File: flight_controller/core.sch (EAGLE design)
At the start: 103 parts, among them J1 M02, J13 MOLEX-3POS, J14 MOLEX-3POS, J15 MOLEX-4POS, J16 MOLEX-3POS, J17 M03, J18 M04, J19 MOLEX-3POS, J2 MOLEX-2POS, J20 MOLEX-4POS, J3 MOLEX-2POS, J4 MOLEX-2POS, J5 MOLEX-2POS, J6 MOLEX-2POS, J7 MOLEX-2POS, J8 MOLEX-2POS, J9 MOLEX-2POS, Q10 EM6K1, Q11 EM6K1, Q2 200mA/50V, Q5 200mA/50V, Q6 200mA/50V, Q7 EM6K1, Q8 EM6K1, U1 MPU-6000QFN-24, U2 MEAS-MS5611, U3 USD-SOCKETNEW, U4 STM32F405, U5 MIC5219 3.3V, Y1 16MHz

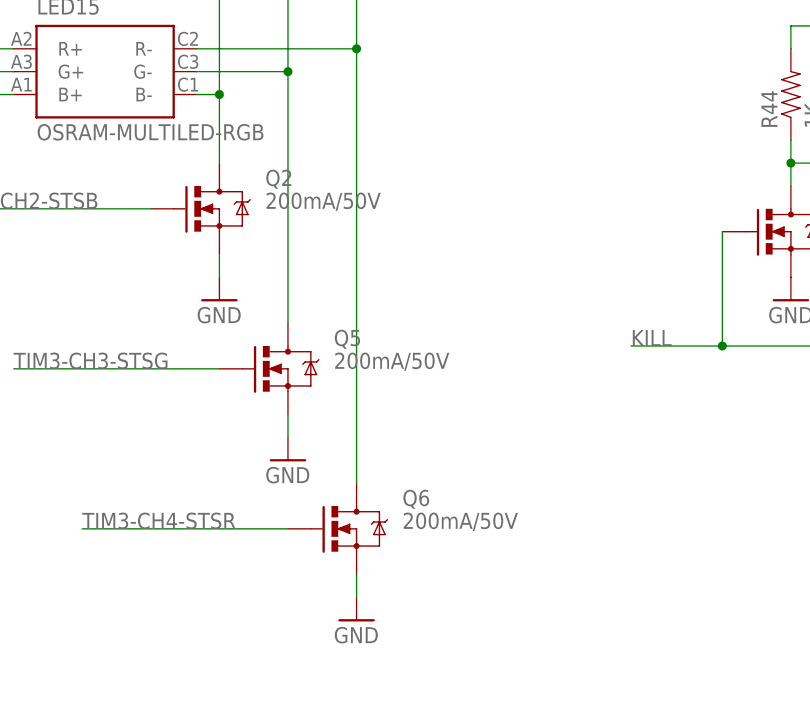
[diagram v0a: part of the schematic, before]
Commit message: Replace LED MOSFETs with dual-channel MOSFETs.
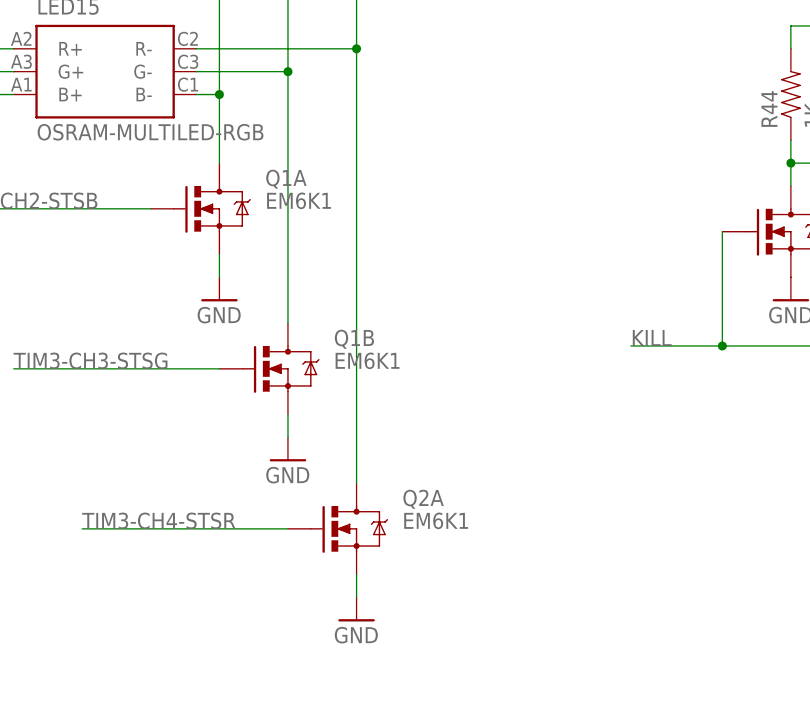
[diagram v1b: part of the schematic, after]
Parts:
- removed Q5, Q6: 200mA/50V, SparkFun-DiscreteSemi:MOSFET-NCHANNELBSS138
- added Q1: EM6K1, OSURC_DiscreteSemi:MOSFET-NCHANNEL-DUALEM6K1
- Q2: value 200mA/50V -> EM6K1; device SparkFun-DiscreteSemi:MOSFET-NCHANNELBSS138 -> OSURC_DiscreteSemi:MOSFET-NCHANNEL-DUALEM6K1
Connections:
- net GND: now also Q1A.S, Q1B.S, Q2A.S; no longer Q2.S, Q5.S, Q6.S
- net N$5: now also Q1A.D; no longer Q2.D
- net N$6: now also Q1B.D; no longer Q5.D
- net N$7: now also Q2A.D; no longer Q6.D
- net TIM3-CH2-STSB: now also Q1A.G; no longer Q2.G
- net TIM3-CH3-STSG: now also Q1B.G; no longer Q5.G
- net TIM3-CH4-STSR: now also Q2A.G; no longer Q6.G
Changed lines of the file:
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@@
 <part name="LED7" library="SparkFun-LED" deviceset="LED" device="0603" value="ORANGE"/>
 <part name="LED14" library="OSURC_LED" deviceset="OSRAM-MULTILED-RGB" device=""/>
-<part name="Q2" library="SparkFun-DiscreteSemi" deviceset="MOSFET-NCHANNEL" device="BSS138" value="200mA/50V"/>
-<part name="Q5" library="SparkFun-DiscreteSemi" deviceset="MOSFET-NCHANNEL" device="BSS138" value="200mA/50V"/>
-<part name="Q6" library="SparkFun-DiscreteSemi" deviceset="MOSFET-NCHANNEL" device="BSS138" value="200mA/50V"/>
 <part name="LED15" library="OSURC_LED" deviceset="OSRAM-MULTILED-RGB" device=""/>
 <part name="GND14" library="SparkFun-Aesthetics" deviceset="GND" device=""/>
@@
 <part name="R48" library="SparkFun" deviceset="RESISTOR" device="0603-RES" value="1K"/>
 <part name="SUPPLY18" library="SparkFun-Aesthetics" deviceset="3.3V" device=""/>
+<part name="Q1" library="OSURC_DiscreteSemi" deviceset="MOSFET-NCHANNEL-DUAL" device="EM6K1" value="EM6K1"/>
+<part name="Q2" library="OSURC_DiscreteSemi" deviceset="MOSFET-NCHANNEL-DUAL" device="EM6K1" value="EM6K1"/>
 </parts>
 <sheets>
@@
 <instance part="LED7" gate="G$1" x="154.94" y="172.72" rot="R90"/>
 <instance part="LED14" gate="G$1" x="254" y="220.98"/>
-<instance part="Q2" gate="G$1" x="266.7" y="182.88"/>
-<instance part="Q5" gate="G$1" x="274.32" y="165.1"/>
-<instance part="Q6" gate="G$1" x="281.94" y="147.32"/>
 <instance part="LED15" gate="G$1" x="254" y="198.12"/>
 <instance part="GND14" gate="1" x="266.7" y="172.72"/>
@@
 <instance part="R48" gate="G$1" x="322.58" y="238.76" rot="R90"/>
 <instance part="SUPPLY18" gate="G$1" x="322.58" y="246.38"/>
+<instance part="Q1" gate="A" x="266.7" y="182.88"/>
+<instance part="Q1" gate="B" x="274.32" y="165.1"/>
+<instance part="Q2" gate="A" x="281.94" y="147.32"/>
 </instances>
 <busses>
@@
 </segment>
 <segment>
-<pinref part="Q2" gate="G$1" pin="S"/>
 <pinref part="GND14" gate="1" pin="GND"/>
 <wire x1="266.7" y1="175.26" x2="266.7" y2="177.8" width="0.1524" layer="91"/>
-</segment>
-<segment>
-<pinref part="Q5" gate="G$1" pin="S"/>
+<pinref part="Q1" gate="A" pin="S"/>
+</segment>
+<segment>
 <pinref part="GND28" gate="1" pin="GND"/>
 <wire x1="274.32" y1="157.48" x2="274.32" y2="160.02" width="0.1524" layer="91"/>
-</segment>
-<segment>
-<pinref part="Q6" gate="G$1" pin="S"/>
+<pinref part="Q1" gate="B" pin="S"/>
+</segment>
+<segment>
 <pinref part="GND29" gate="1" pin="GND"/>
 <wire x1="281.94" y1="139.7" x2="281.94" y2="142.24" width="0.1524" layer="91"/>
+<pinref part="Q2" gate="A" pin="S"/>
 </segment>
 <segment>
@@
 <wire x1="266.7" y1="165.1" x2="243.84" y2="165.1" width="0.1524" layer="91"/>
 <label x="243.84" y="165.1" size="1.778" layer="95"/>
-<pinref part="Q5" gate="G$1" pin="G"/>
+<pinref part="Q1" gate="B" pin="G"/>
 </segment>
 </net>
@@
 <segment>
 <pinref part="LED15" gate="G$1" pin="B-"/>
-<pinref part="Q2" gate="G$1" pin="D"/>
 <wire x1="264.16" y1="195.58" x2="266.7" y2="195.58" width="0.1524" layer="91"/>
 <wire x1="266.7" y1="195.58" x2="266.7" y2="187.96" width="0.1524" layer="91"/>
@@
 <wire x1="266.7" y1="218.44" x2="266.7" y2="195.58" width="0.1524" layer="91"/>
 <junction x="266.7" y="195.58"/>
+<pinref part="Q1" gate="A" pin="D"/>
 </segment>
 </net>
@@
 <segment>
 <pinref part="LED15" gate="G$1" pin="G-"/>
-<pinref part="Q5" gate="G$1" pin="D"/>
 <wire x1="264.16" y1="198.12" x2="274.32" y2="198.12" width="0.1524" layer="91"/>
 <wire x1="274.32" y1="198.12" x2="274.32" y2="170.18" width="0.1524" layer="91"/>
@@
 <wire x1="274.32" y1="220.98" x2="274.32" y2="198.12" width="0.1524" layer="91"/>
 <junction x="274.32" y="198.12"/>
+<pinref part="Q1" gate="B" pin="D"/>
 </segment>
 </net>
@@
 <segment>
 <pinref part="LED15" gate="G$1" pin="R-"/>
-<pinref part="Q6" gate="G$1" pin="D"/>
 <wire x1="264.16" y1="200.66" x2="281.94" y2="200.66" width="0.1524" layer="91"/>
 <wire x1="281.94" y1="200.66" x2="281.94" y2="152.4" width="0.1524" layer="91"/>
@@
 <wire x1="281.94" y1="223.52" x2="281.94" y2="200.66" width="0.1524" layer="91"/>
 <junction x="281.94" y="200.66"/>
+<pinref part="Q2" gate="A" pin="D"/>
 </segment>
 </net>
@@
 <wire x1="236.22" y1="182.88" x2="259.08" y2="182.88" width="0.1524" layer="91"/>
 <label x="236.22" y="182.88" size="1.778" layer="95"/>
-<pinref part="Q2" gate="G$1" pin="G"/>
+<pinref part="Q1" gate="A" pin="G"/>
 </segment>
 </net>
@@
 <wire x1="274.32" y1="147.32" x2="251.46" y2="147.32" width="0.1524" layer="91"/>
 <label x="251.46" y="147.32" size="1.778" layer="95"/>
-<pinref part="Q6" gate="G$1" pin="G"/>
-</segment>
-</net>
+<pinref part="Q2" gate="A" pin="G"/>
+</segment>
+</net>

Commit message: Remove 5V regulator todo and add reverse voltage protection.
Board will need 5V input from external regulator.
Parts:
- added J10: MOLEX-2POS, aerial:MOLEX-2POS
- added Q3: MOSFET-PCHANNEL-AON6407, OSURC_DiscreteSemi:MOSFET-PCHANNEL-AON6407
- Q1, Q10, Q11, Q2, Q7, Q8: device OSURC_DiscreteSemi:MOSFET-NCHANNEL-DUALEM6K1 -> OSURC_DiscreteSemi:MOSFET-NCHANNEL-DUAL-EM6K1
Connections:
- new net VIN: J10.1, Q3.D
- net 5V: now also Q3.S
- net GND: now also J10.2, Q3.G
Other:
- note added: "1K pullup on KILL pulls TIM1 and TIM4 channels down until the XBee deasserts KILL."
- note added: "5V in"
- note added: "Protection"
- note added: "Reverse Voltage"
- note added: "TODO: consider replacing with Molex Duraclik"
- note added: "TVS"
- note removed: "1K pullup on KILL keeps these N-ch MOSFETS on, pulling TIM1 and TIM4 channels down, until the XBee deasserts KILL."
- note removed: "5V REG"

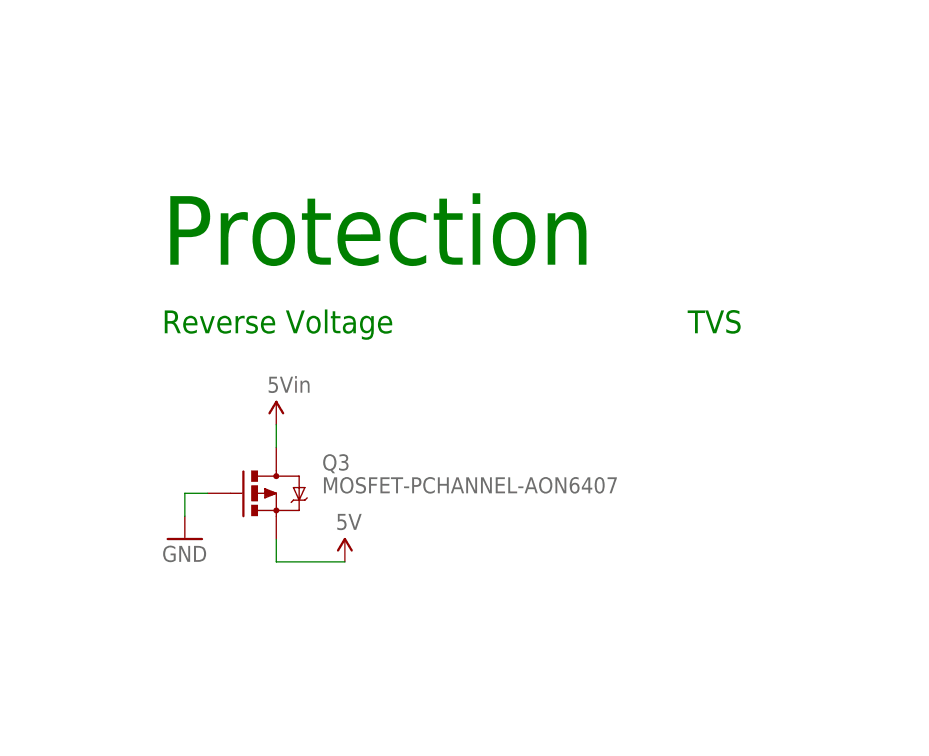
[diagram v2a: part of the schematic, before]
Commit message: Add TVS/RVP circuit.
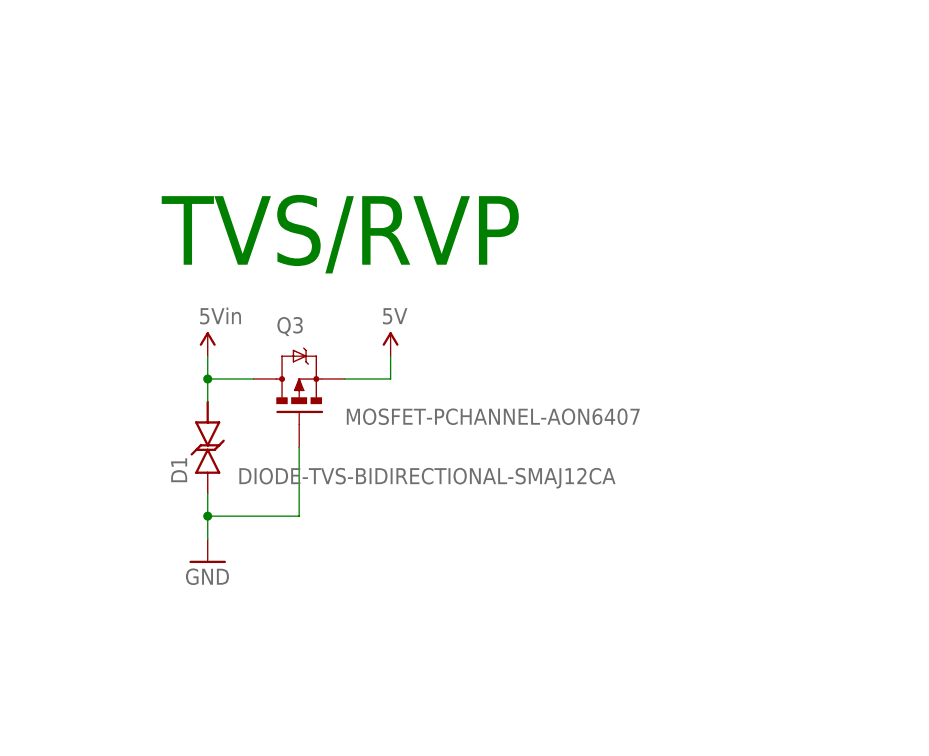
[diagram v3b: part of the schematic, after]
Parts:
- added D1: DIODE-TVS-BIDIRECTIONAL-SMAJ12CA, OSURC_DiscreteSemi:DIODE-TVS-BIDIRECTIONAL-SMAJ12CA
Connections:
- net GND: now also D1.1
- net VIN: now also D1.2
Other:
- note added: "TVS/RVP"
- note removed: "Protection"
- note removed: "Reverse Voltage"
- note removed: "TVS"
- moved on the sheet: Q3
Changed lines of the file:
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@@
 <part name="GND22" library="SparkFun-Aesthetics" deviceset="GND" device=""/>
 <part name="SUPPLY22" library="SparkFun-Aesthetics" deviceset="VIN" device="" value="5Vin"/>
+<part name="D1" library="OSURC_DiscreteSemi" deviceset="DIODE-TVS-BIDIRECTIONAL" device="-SMAJ12CA"/>
 </parts>
 <sheets>
@@
 the XBee deasserts KILL.</text>
 <text x="317.5" y="-403.86" size="7.62" layer="91">5V in</text>
-<text x="129.54" y="-73.66" size="7.62" layer="91">Protection</text>
+<text x="129.54" y="-73.66" size="7.62" layer="91">TVS/RVP</text>
 <text x="317.5" y="-439.42" size="1.778" layer="98">TODO: consider replacing with Molex Duraclik</text>
-<text x="129.54" y="-81.28" size="2.54" layer="91">Reverse Voltage</text>
-<text x="187.96" y="-81.28" size="2.54" layer="91">TVS</text>
 </plain>
 <instances>
@@
 <instance part="J10" gate="G$1" x="327.66" y="-421.64"/>
 <instance part="GND9" gate="1" x="320.04" y="-429.26"/>
-<instance part="Q3" gate="G$1" x="142.24" y="-99.06"/>
-<instance part="SUPPLY19" gate="G$1" x="142.24" y="-91.44"/>
-<instance part="SUPPLY21" gate="G$1" x="149.86" y="-106.68"/>
-<instance part="GND22" gate="1" x="132.08" y="-104.14"/>
+<instance part="Q3" gate="G$1" x="144.78" y="-86.36" smashed="yes" rot="R90">
+<attribute name="NAME" x="142.24" y="-81.28" size="1.778" layer="95"/>
+<attribute name="VALUE" x="149.86" y="-91.44" size="1.778" layer="96"/>
+</instance>
+<instance part="SUPPLY19" gate="G$1" x="134.62" y="-83.82"/>
+<instance part="SUPPLY21" gate="G$1" x="154.94" y="-83.82"/>
+<instance part="GND22" gate="1" x="134.62" y="-106.68"/>
 <instance part="SUPPLY22" gate="G$1" x="320.04" y="-414.02"/>
+<instance part="D1" gate="G$1" x="134.62" y="-93.98" smashed="yes" rot="R90">
+<attribute name="NAME" x="132.334" y="-98.044" size="1.778" layer="95" rot="R90"/>
+<attribute name="VALUE" x="137.922" y="-98.044" size="1.778" layer="96"/>
+</instance>
 </instances>
 <busses>
@@
 </segment>
 <segment>
+<pinref part="GND22" gate="1" pin="GND"/>
+<wire x1="134.62" y1="-104.14" x2="134.62" y2="-101.6" width="0.1524" layer="91"/>
 <pinref part="Q3" gate="G$1" pin="G"/>
-<pinref part="GND22" gate="1" pin="GND"/>
-<wire x1="134.62" y1="-99.06" x2="132.08" y2="-99.06" width="0.1524" layer="91"/>
-<wire x1="132.08" y1="-99.06" x2="132.08" y2="-101.6" width="0.1524" layer="91"/>
+<wire x1="134.62" y1="-101.6" x2="134.62" y2="-99.06" width="0.1524" layer="91"/>
+<wire x1="144.78" y1="-93.98" x2="144.78" y2="-101.6" width="0.1524" layer="91"/>
+<wire x1="144.78" y1="-101.6" x2="134.62" y2="-101.6" width="0.1524" layer="91"/>
+<junction x="134.62" y="-101.6"/>
+<pinref part="D1" gate="G$1" pin="1"/>
 </segment>
 </net>
@@
 <segment>
 <pinref part="Q3" gate="G$1" pin="S"/>
-<wire x1="142.24" y1="-104.14" x2="142.24" y2="-106.68" width="0.1524" layer="91"/>
+<wire x1="149.86" y1="-86.36" x2="154.94" y2="-86.36" width="0.1524" layer="91"/>
 <pinref part="SUPPLY21" gate="G$1" pin="5V"/>
-<wire x1="142.24" y1="-106.68" x2="149.86" y2="-106.68" width="0.1524" layer="91"/>
+<wire x1="154.94" y1="-86.36" x2="154.94" y2="-83.82" width="0.1524" layer="91"/>
 </segment>
 </net>
@@
 <net name="VIN" class="0">
 <segment>
-<pinref part="SUPPLY19" gate="G$1" pin="VIN"/>
-<pinref part="Q3" gate="G$1" pin="D"/>
-<wire x1="142.24" y1="-91.44" x2="142.24" y2="-93.98" width="0.1524" layer="91"/>
-</segment>
-<segment>
 <pinref part="J10" gate="G$1" pin="1"/>
 <wire x1="322.58" y1="-419.1" x2="320.04" y2="-419.1" width="0.1524" layer="91"/>
@@
 <pinref part="SUPPLY22" gate="G$1" pin="VIN"/>
 </segment>
-</net>
+<segment>
+<pinref part="SUPPLY19" gate="G$1" pin="VIN"/>
+<wire x1="134.62" y1="-83.82" x2="134.62" y2="-86.36" width="0.1524" layer="91"/>
+<pinref part="Q3" gate="G$1" pin="D"/>
+<wire x1="134.62" y1="-86.36" x2="134.62" y2="-88.9" width="0.1524" layer="91"/>
+<wire x1="134.62" y1="-86.36" x2="139.7" y2="-86.36" width="0.1524" layer="91"/>
+<junction x="134.62" y="-86.36"/>
+<pinref part="D1" gate="G$1" pin="2"/>
+</segment>
+</net>

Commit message: Implement MPU-9250.
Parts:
- removed C19: 2.2nF, SparkFun-Capacitors:2.2NF/2200PF-50V-10%(0603)
- removed U1: MPU-6000QFN-24, SparkFun-Sensors:MPU-6000QFN-24
- added C17: 0.1uF, SparkFun-Capacitors:0.1UF-25V-5%(0603)
- added U6: (no value), OSURC_Sensors:MPU-9250-QFN-24-NP
- C12: value 0.1uF -> 10nF; device SparkFun-Capacitors:0.1UF-25V-5%(0603) -> SparkFun-Capacitors:10NF/10000PF-50V-10%(0603)
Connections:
- removed net MPU-CPOUT: C19.1, U1.CPOUT
- removed net MPU-REGOUT: C12.1, U1.REGOUT
- removed net SPISS-MPU6000: U1.CS, U4.GPIO.PC14
- new net MPU9250-REGOUT: C17.1, U6.REGOUT
- new net SPISS-MPU9250: U4.GPIO.PC14, U6.NCS
- net 3.3V: now also C12.1, U6.RESV@1, U6.VDD, U6.VDDIO; no longer U1.VDD
- net GND: now also C17.2, U6.FSYNC, U6.GND, U6.RESV@20; no longer C19.2, U1.GND
- net SPI1-MISO: now also U6.AD0/SDO; no longer U1.AD0/SDO
- net SPI1-MOSI: now also U6.SDA/SDI; no longer U1.SDA/SDI
- net SPI1-SCK: now also U6.SCL/SCLK; no longer U1.SCL/SCLK
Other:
- note added: "MPU-9250"
- note added: "REG"
- note added: "VDD"
- note added: "VDDIO"
- note removed: "MPU-6000"
- moved on the sheet: C11, C12, C14

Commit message: Move some things around.
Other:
- note added: "TODO(yoos): Add digital I/O connectors"
- note removed: "TODO(yoos): Add external connectors for some digital I/O"
- moved on the sheet: C11, C12, C14, C17, LED1, LED10, LED11, LED12, LED13, LED14, LED15, LED2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

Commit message: Add digital I/O pins, remove some LEDs, rearrange stuff.
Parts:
- removed LED1, LED2, LED3, LED4: ORANGE, SparkFun-LED:LED0603
- removed R14, R15, R21, R22: 680, SparkFun-Passives:RESISTOR0603-RES
- added J11, J12, J21, J22: MOLEX-2POS, aerial:MOLEX-2POS
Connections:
- removed net N$27: LED2.A, R15.2
- removed net N$28: LED1.A, R14.2
- removed net N$29: LED3.A, R21.2
- removed net N$30: LED4.A, R22.2
- net GND: now also J11.2, J12.2, J21.2, J22.2; no longer LED1.C, LED2.C, LED3.C, LED4.C
- net PA4: now also J11.1; no longer R15.1
- net PA5: now also J12.1; no longer R14.1
- net PC4: now also J21.1; no longer R21.1
- net PC5: now also J22.1; no longer R22.1
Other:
- note added: "Debug"
- note added: "Digital"
- note added: "Status"
- note removed: "Dig I/O"
- note removed: "Status LED"
- note removed: "TODO(yoos): Add digital I/O connectors"
- moved on the sheet: J1, J10, J13, J14, J15, J16, J17, J18, J19, J2, J20, J3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

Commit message: Resolve most ERC errors.
Two warnings for unused F4's B12 and C15.
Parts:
- removed J9: MOLEX-2POS, aerial:MOLEX-2POS
- U6: value (none) -> MPU-9250-QFN-24-NP
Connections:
- removed net N$1: U3.VCC
- removed net TIM3-CH1: J9.1
- removed net TIM3-CH2-STSB: Q1A.G
- removed net TIM3-CH4-STSR: Q2A.G
- net 3.3V: now also U3.VCC; no longer J13.2, J14.2
- net 5V: now also J13.2, J14.2
- net GND: no longer J9.2
- net TIM3-CH2-STSR: now also Q2A.G
- net TIM3-CH4-STSB: now also Q1A.G
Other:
- note added: "TODO: B12 and C15 unused"
- moved on the sheet: J11, J12, J13, J14, J21, J22, R1, R16, R17, R5
